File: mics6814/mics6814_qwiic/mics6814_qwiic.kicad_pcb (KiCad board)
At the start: 2 copper layers, 25.4 x 17.8 mm, 22 parts, among them J1 QWIIC_CONNECTORJS-1MM, J2 QWIIC_CONNECTORJS-1MM, Q1 MOSFET_PCH-DMG2307L, U1 ADS1115, U2 74HC1G04

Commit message: Board update
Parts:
- added JP7: PULL UP SDA, Sparkfun-Jumpers:SMT-JUMPER_2_NC_TRACE_SILK, B.Cu at (120.8, 102.2)
- added JP8: PULL UP SCL, Sparkfun-Jumpers:SMT-JUMPER_2_NC_TRACE_SILK, B.Cu at (118.6, 106.2)
- added R7: 10k, Sparkfun-Resistors:0805, F.Cu at (120.1, 102.7)
- added R8: 10k, Sparkfun-Resistors:0805, F.Cu at (117.6, 106.1)
- JP2: value LED -> Power LED
- JP4: value LEDSW -> HEAT LED
- moved R4 0.48 mm to (107.8, 110.7)
- renumbered C1 to 1uF, L1 to 1uH
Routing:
- net GND: track 20.5 -> 42.9 mm
- net /SCL: track 26.9 -> 35.3 mm, vias 2 -> 3
- net +3V3: track 55.8 -> 61.7 mm
- net Net-(JP7-Pad1): track 0.00 -> 3.24 mm, vias 0 -> 1
- net Net-(JP8-Pad1): track 0.00 -> 3.20 mm, vias 0 -> 1
- net /SDA: track 22.4 -> 23.3 mm
- net /NO2_R: track 6.46 -> 6.98 mm
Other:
- board text added: "0x48 (default)"
- board text added: "0x49"
- board text added: "0x4a"
- board text added: "0x4b"
- board text added: "3V3"
- board text added: "ADDR"
- board text added: "HEAT"
- board text added: "LED"
- board text added: "MICS6814 breakout board V1.0 by jdexyz"
- board text added: "MOS"
- board text added: "PMOS"
- board text added: "PULL UP"
- board text added: "qwiic"

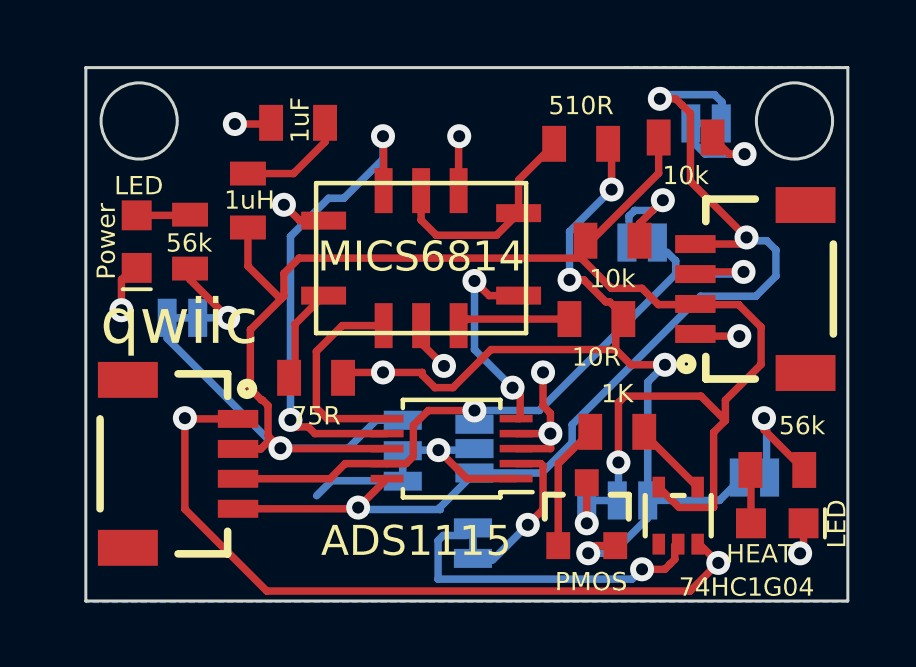
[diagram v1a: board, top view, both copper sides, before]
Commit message: Rounded corners
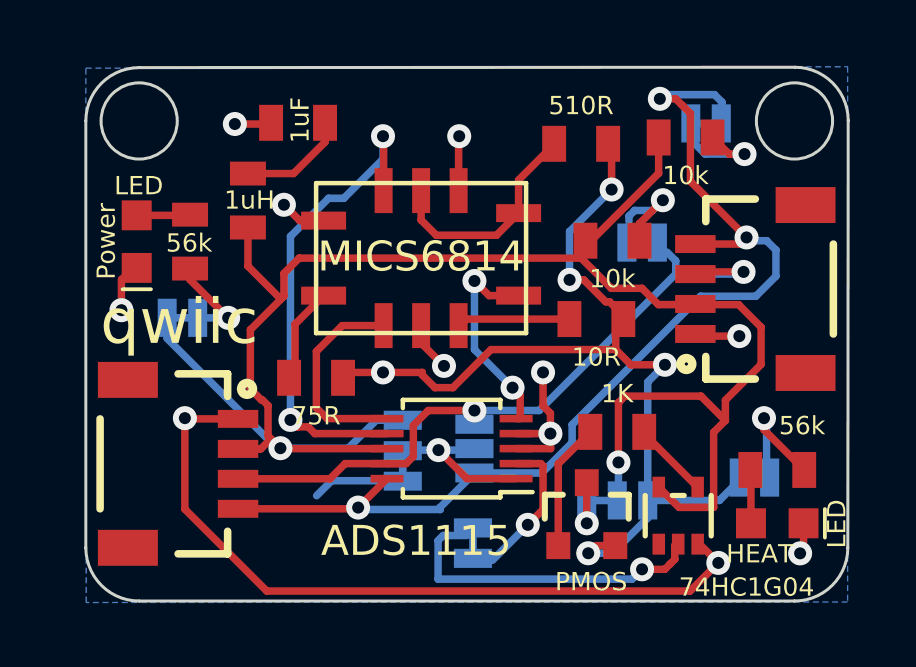
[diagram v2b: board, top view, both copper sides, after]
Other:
- outline, holes or cut-outs redrawn
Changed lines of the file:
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@@
       (net 3 "+3V3") (pinfunction "2") (pintype "passive") (solder_mask_margin 0.1016))
   )
-  (gr_rect (start 100.076 100.33) (end 125.476 118.11) (layer "Edge.Cuts") (width 0.1) (fill none))
+  (gr_arc (start 100.076 102.108) (mid 100.596764 100.850764) (end 101.854 100.33) (layer "Edge.Cuts") (width 0.1))
+  (gr_line (start 100.076 102.108) (end 100.076 116.332) (layer "Edge.Cuts") (width 0.1))
   (gr_circle (center 101.854 102.108) (end 103.124 102.108) (layer "Edge.Cuts") (width 0.1) (fill none))
   (gr_circle (center 123.698 102.108) (end 124.968 102.108) (layer "Edge.Cuts") (width 0.1) (fill none))
+  (gr_line (start 123.710764 100.317236) (end 101.854 100.33) (layer "Edge.Cuts") (width 0.1))
+  (gr_arc (start 123.710764 100.317236) (mid 124.968 100.838) (end 125.488764 102.095236) (layer "Edge.Cuts") (width 0.1))
+  (gr_arc (start 125.476 116.332) (mid 124.955236 117.589236) (end 123.698 118.11) (layer "Edge.Cuts") (width 0.1))
+  (gr_line (start 125.476 116.332) (end 125.488764 102.095236) (layer "Edge.Cuts") (width 0.1))
+  (gr_arc (start 101.854 118.11) (mid 100.596764 117.589236) (end 100.076 116.332) (layer "Edge.Cuts") (width 0.1))
+  (gr_line (start 101.854 118.11) (end 123.698 118.11) (layer "Edge.Cuts") (width 0.1))
   (gr_text "0x48 (default)" (at 106.71 114.13) (layer "B.SilkS")
     (effects (font (size 0.5 0.5) (thickness 0.125)) (justify mirror))
